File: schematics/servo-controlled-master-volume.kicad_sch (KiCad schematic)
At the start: 14 parts, among them J10 Midi In, M1 Servo, U1 6N138

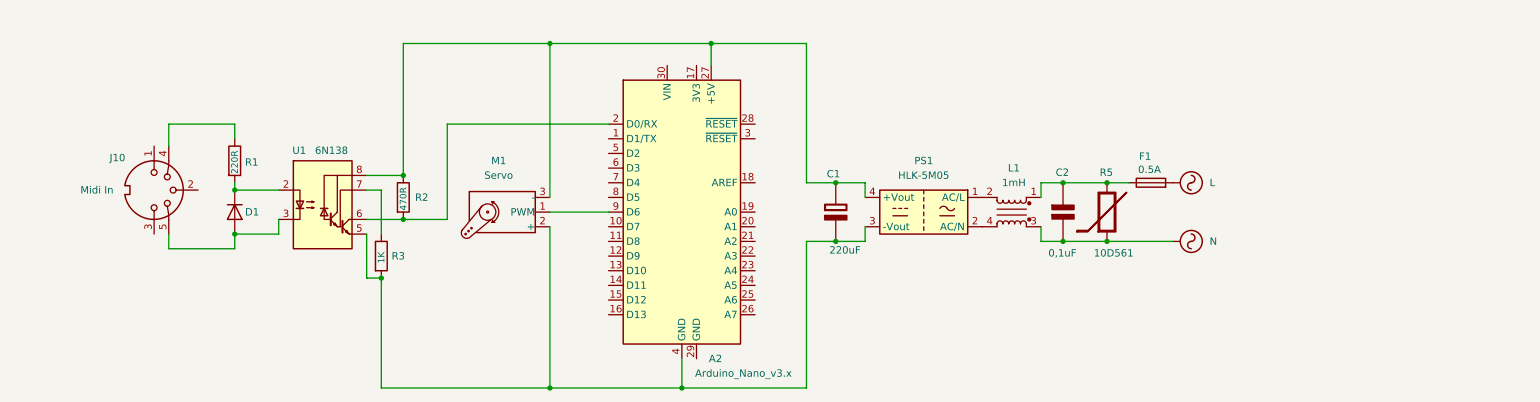
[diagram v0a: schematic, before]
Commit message: added partial schematics
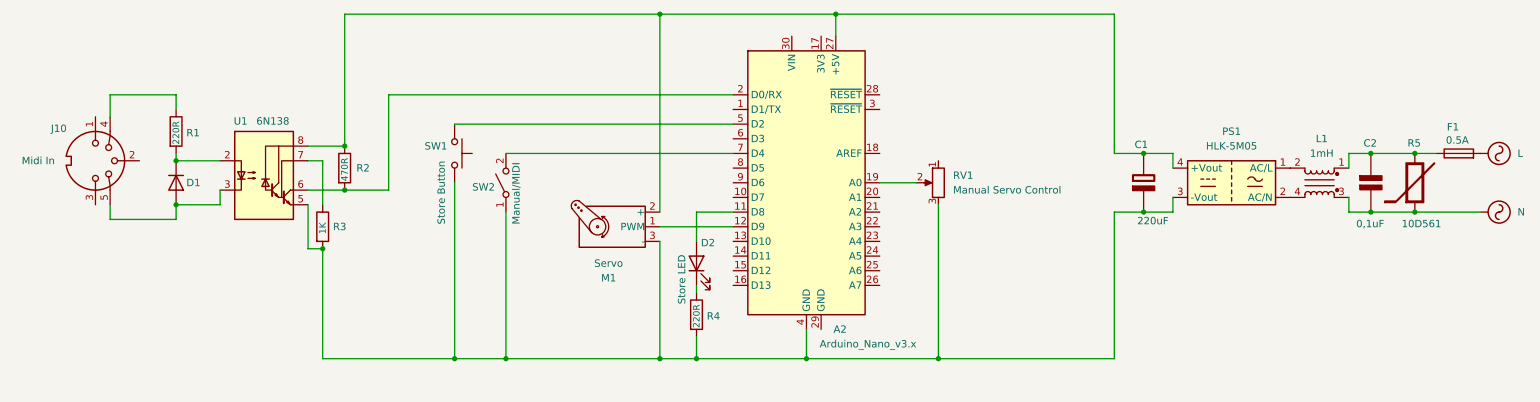
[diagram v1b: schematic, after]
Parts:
- added D2: Store LED, symbol Device:LED
- added R4: 220R, symbol Device:R
- added RV1: Manual Servo Control, symbol Device:R_Potentiometer
- added SW1: Store Button, symbol Switch:SW_Push
- added SW2: Manual/MIDI, symbol Switch:SW_SPST
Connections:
- net at A2.4 (GND), C1.2 (-), PS1.3 (-Vout)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: now also M1.3 (-), R4.2, RV1.3, SW1.1, SW2.1 (A); no longer M1.2 (+)
- net at A2.27 (+5V), C1.1 (+), PS1.4 (+Vout)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: now also M1.2 (+); no longer M1.3 (-)
- net at A2.11 (D8): now also D2.2 (A)
- net at A2.12 (D9): now also M1.1 (PWM)
- net at A2.19 (A0): now also RV1.2
- net at A2.5 (D2): now also SW1.2
- net at A2.7 (D4): now also SW2.2 (B)
- net at A2.9 (D6): no longer M1.1 (PWM)
- new net: D2.1 (K), R4.1
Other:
- moved on the sheet: A2, C1, C2, D1, F1, J10, L1, M1, PS1, R1, R2, R3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
